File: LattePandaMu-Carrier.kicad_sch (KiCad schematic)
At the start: 0 parts

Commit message: feat: Added hierarchical sheets
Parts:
- added FID78, FID79: Fiducial, symbol Mechanical:Fiducial
- added H1, H2, H3, H4: MountingHole_Pad, symbol Mechanical:MountingHole_Pad
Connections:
- new net GND: H1.1, H2.1, H3.1, H4.1
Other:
- added sheet Fan (fan.kicad_sch)
- added sheet GPIO (gpio.kicad_sch)
- added sheet Gigabit Ethernet (ethernet.kicad_sch)
- added sheet HDMI (hdmi.kicad_sch)
- added sheet LattePanda Module (LattePanda_Module.kicad_sch)
- added sheet M.2 M Key (m2_em_key.kicad_sch)
- added sheet PCIe x4 (picex4.kicad_sch)
- added sheet Power Supply (psu.kicad_sch)
- added sheet USB 2.0 & 3.0 (usb_2_3.kicad_sch)

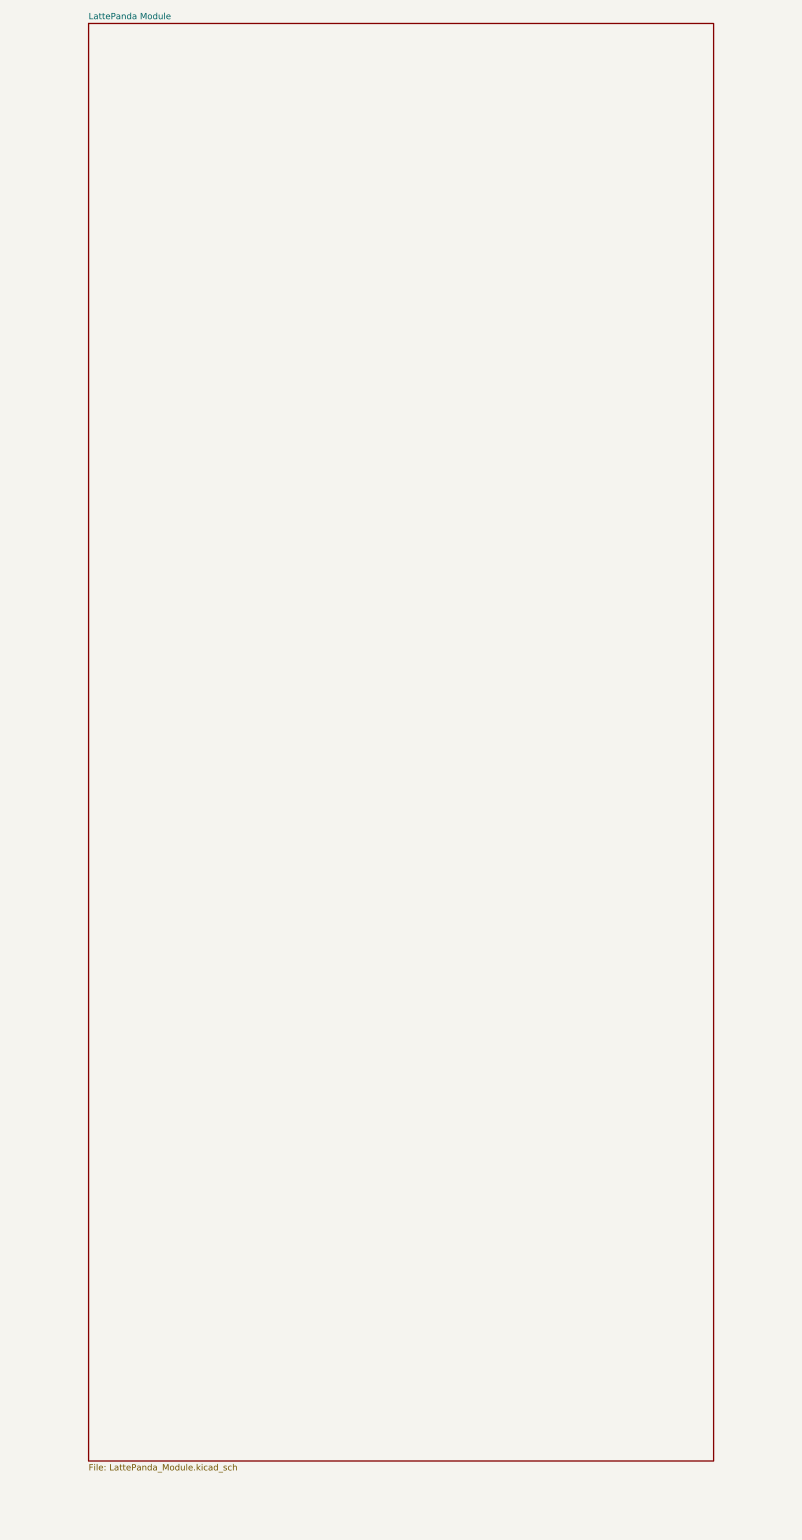
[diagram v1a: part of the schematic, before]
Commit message: feat: Added hierarchical sheets and pins
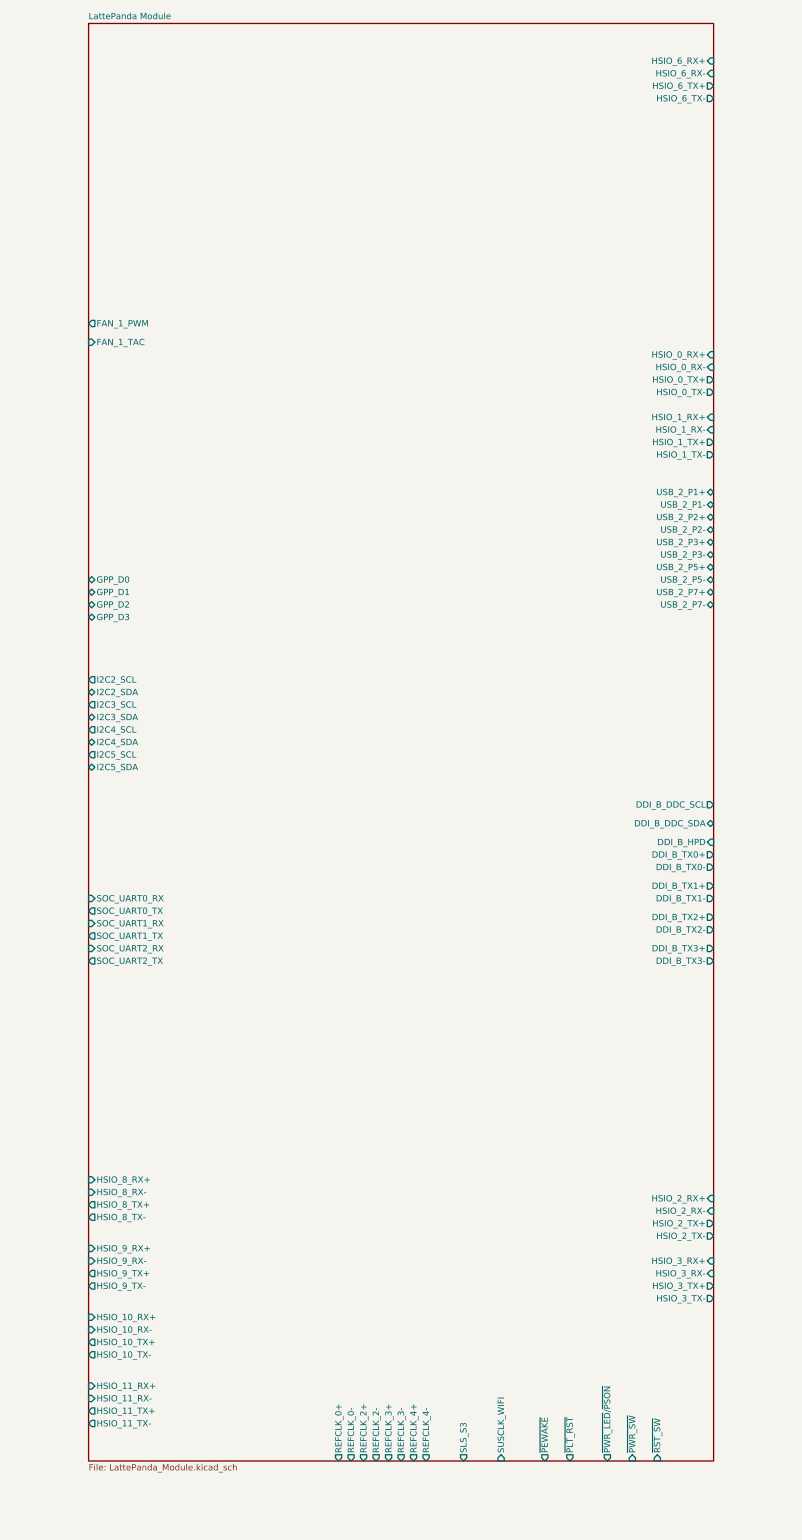
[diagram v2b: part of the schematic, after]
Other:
- sheet LattePanda Module ports: added DDI_B_DDC_SCL, DDI_B_DDC_SDA, DDI_B_HPD, DDI_B_TX0+, DDI_B_TX0-, DDI_B_TX1+, DDI_B_TX1-, DDI_B_TX2+, DDI_B_TX2-, DDI_B_TX3+, DDI_B_TX3-, FAN_1_PWM, FAN_1_TAC, GPP_D0, GPP_D1, GPP_D2, GPP_D3, HSIO_0_RX+, HSIO_0_RX-, HSIO_0_TX+, HSIO_0_TX-, HSIO_10_RX+, HSIO_10_RX-, HSIO_10_TX+, HSIO_10_TX-, HSIO_11_RX+, HSIO_11_RX-, HSIO_11_TX+, HSIO_11_TX-, HSIO_1_RX+, HSIO_1_RX-, HSIO_1_TX+, HSIO_1_TX-, HSIO_2_RX+, HSIO_2_RX-, HSIO_2_TX+, HSIO_2_TX-, HSIO_3_RX+, HSIO_3_RX-, HSIO_3_TX+, HSIO_3_TX-, HSIO_6_RX+, HSIO_6_RX-, HSIO_6_TX+, HSIO_6_TX-, HSIO_8_RX+, HSIO_8_RX-, HSIO_8_TX+, HSIO_8_TX-, HSIO_9_RX+, HSIO_9_RX-, HSIO_9_TX+, HSIO_9_TX-, I2C2_SCL, I2C2_SDA, I2C3_SCL, I2C3_SDA, I2C4_SCL, I2C4_SDA, I2C5_SCL, I2C5_SDA, REFCLK_0+, REFCLK_0-, REFCLK_2+, REFCLK_2-, REFCLK_3+, REFCLK_3-, REFCLK_4+, REFCLK_4-, SLS_S3, SOC_UART0_RX, SOC_UART0_TX, SOC_UART1_RX, SOC_UART1_TX, SOC_UART2_RX, SOC_UART2_TX, SUSCLK_WIFI, USB_2_P1+, USB_2_P1-, USB_2_P2+, USB_2_P2-, USB_2_P3+, USB_2_P3-, USB_2_P5+, USB_2_P5-, USB_2_P7+, USB_2_P7-, ~{PEWAKE}, ~{PLT_RST}, ~{PWR_LED}/~{PSON}, ~{PWR_SW}, ~{RST_SW}; removed none

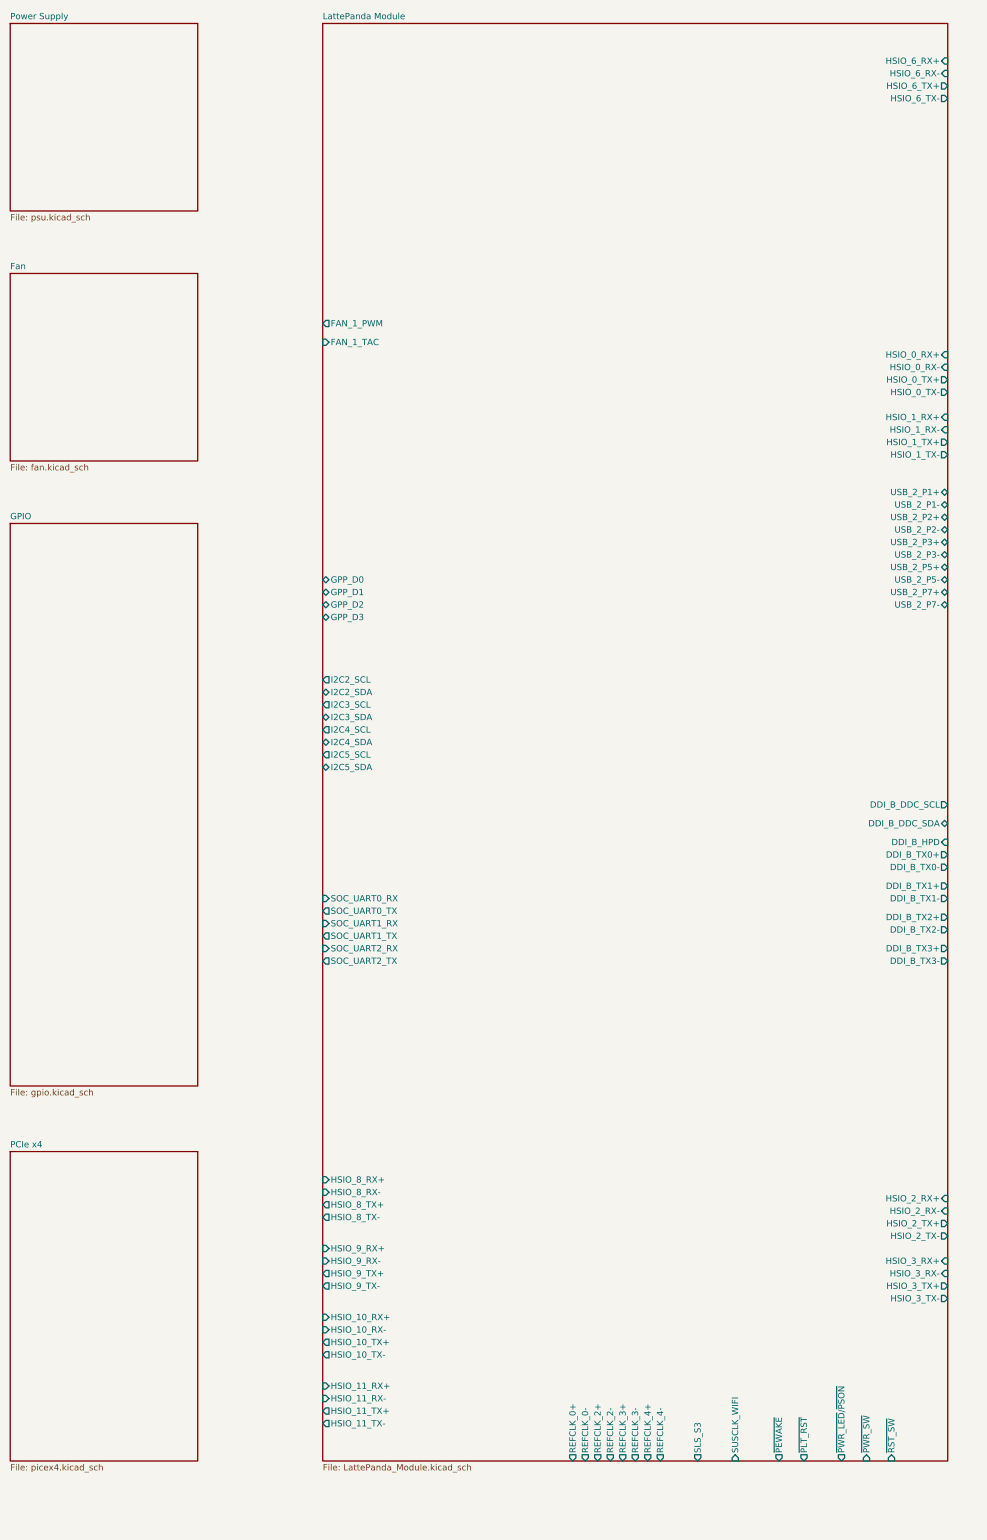
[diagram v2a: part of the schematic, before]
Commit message: feat(psu): Connected psu hierarchical pins to LattePanda sheet
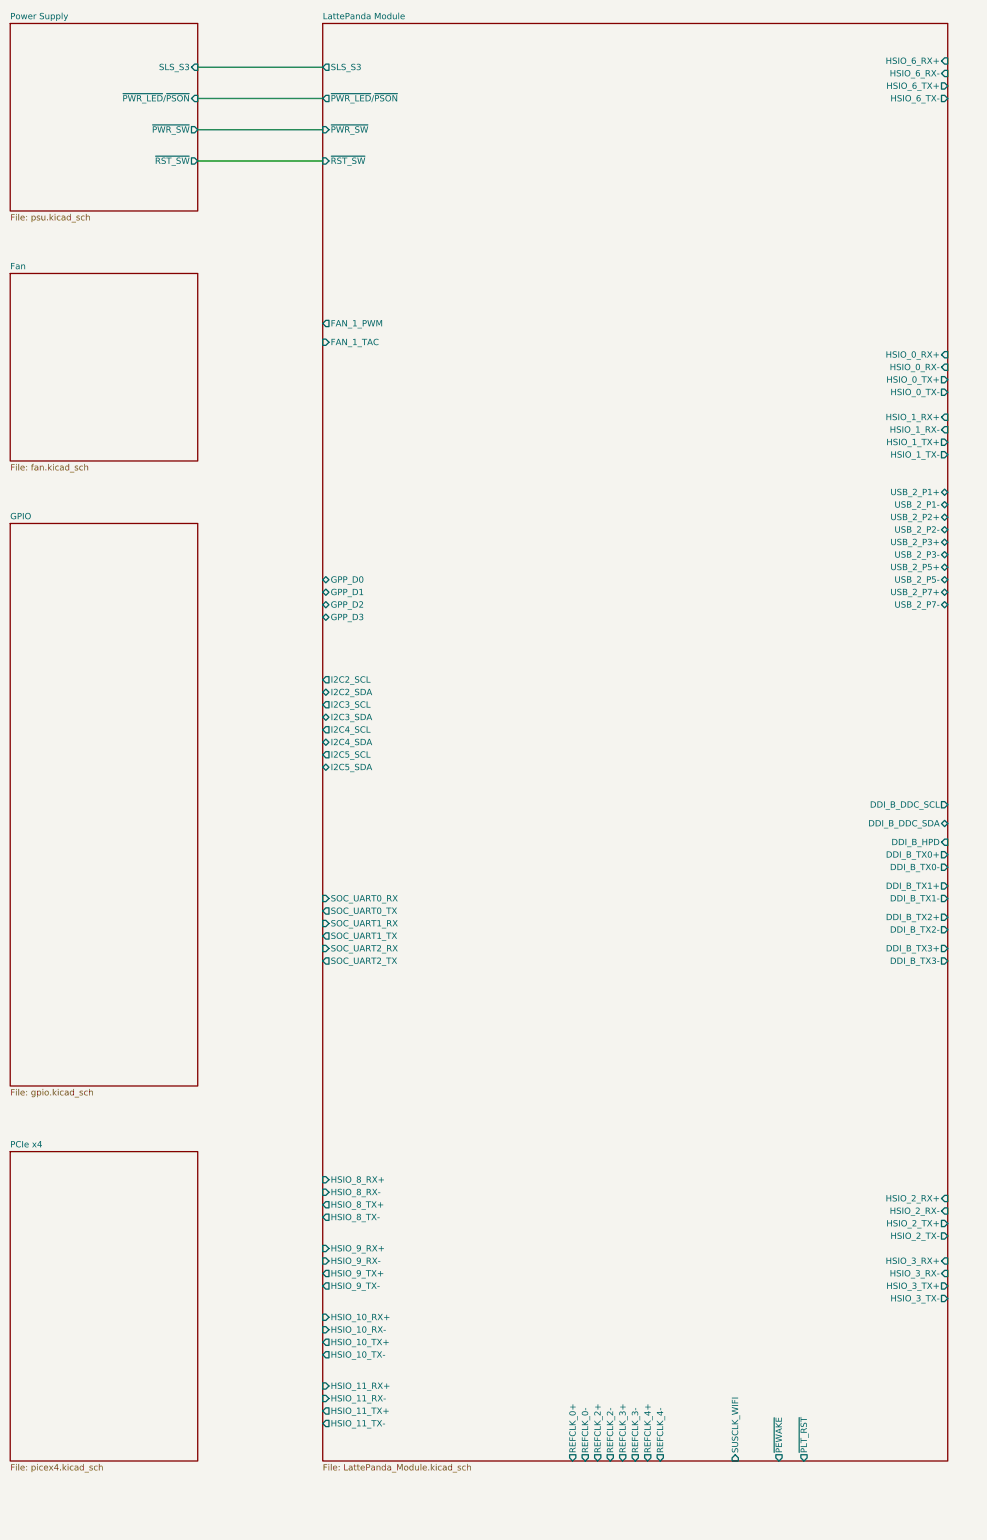
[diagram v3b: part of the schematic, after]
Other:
- sheet Power Supply ports: added SLS_S3, ~{PWR_LED}/~{PSON}, ~{PWR_SW}, ~{RST_SW}; removed none
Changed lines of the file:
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@@
 		(rev "1")
+	)
+	(wire
+		(pts
+			(xy 165.1 66.04) (xy 190.5 66.04)
+		)
+		(stroke
+			(width 0)
+			(type default)
+		)
+	)
+	(wire
+		(pts
+			(xy 165.1 78.74) (xy 190.5 78.74)
+		)
+		(stroke
+			(width 0)
+			(type default)
+		)
+	)
+	(wire
+		(pts
+			(xy 165.1 59.69) (xy 190.5 59.69)
+		)
+		(stroke
+			(width 0)
+			(type default)
+		)
+	)
+	(wire
+		(pts
+			(xy 165.1 72.39) (xy 190.5 72.39)
+		)
+		(stroke
+			(width 0)
+			(type default)
+		)
 	)
 	(symbol
@@
 			)
 		)
+		(pin "SLS_S3" input
+			(at 165.1 59.69 0)
+			(effects
+				(font
+					(size 1.27 1.27)
+				)
+				(justify right)
+			)
+		)
+		(pin "~{PWR_LED}{slash}~{PSON}" input
+			(at 165.1 66.04 0)
+			(effects
+				(font
+					(size 1.27 1.27)
+				)
+				(justify right)
+			)
+		)
+		(pin "~{PWR_SW}" output
+			(at 165.1 72.39 0)
+			(effects
+				(font
+					(size 1.27 1.27)
+				)
+				(justify right)
+			)
+		)
+		(pin "~{RST_SW}" output
+			(at 165.1 78.74 0)
+			(effects
+				(font
+					(size 1.27 1.27)
+				)
+				(justify right)
+			)
+		)
 		(instances
 			(project "LattePandaMu-Carrier"
@@
 		)
 		(pin "SLS_S3" output
-			(at 266.7 342.9 270)
+			(at 190.5 59.69 180)
 			(effects
 				(font
@@
 		)
 		(pin "~{PWR_LED}{slash}~{PSON}" output
-			(at 295.91 342.9 270)
+			(at 190.5 66.04 180)
 			(effects
 				(font
@@
 		)
 		(pin "~{PWR_SW}" input
-			(at 300.99 342.9 270)
+			(at 190.5 72.39 180)
 			(effects
 				(font
@@
 		)
 		(pin "~{RST_SW}" input
-			(at 306.07 342.9 270)
-			(effects
-				(font
+			(at 190.5 78.74 180)
+			(effects
+				(font

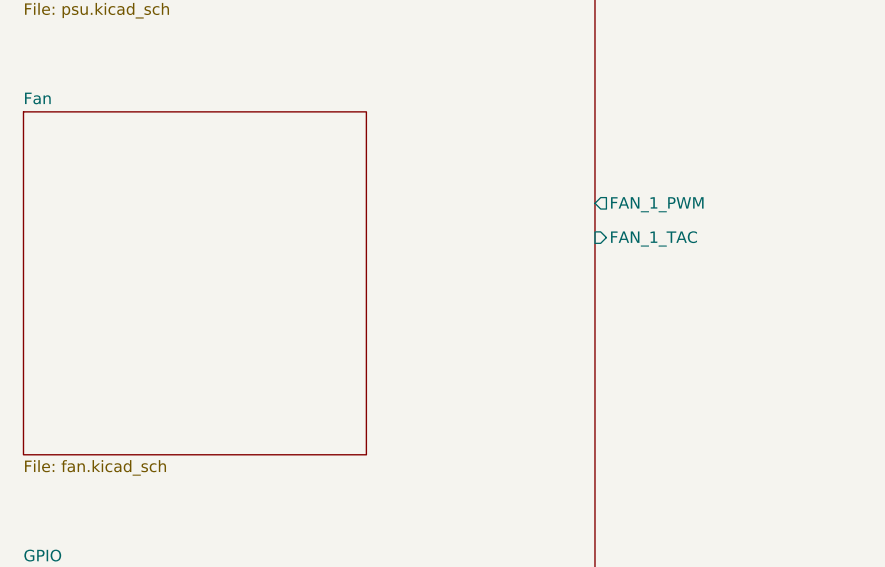
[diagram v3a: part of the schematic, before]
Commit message: feat(fan): Added fan circuit and connected sheet pins
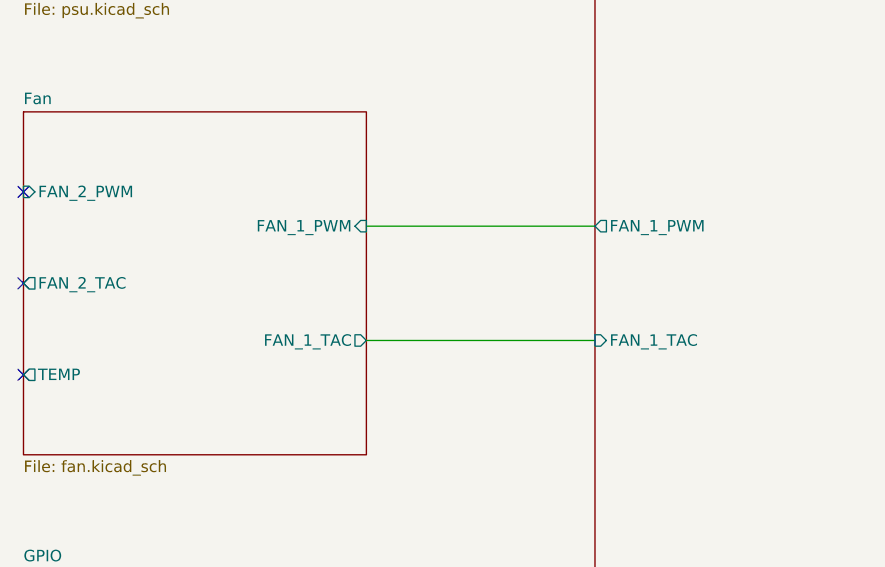
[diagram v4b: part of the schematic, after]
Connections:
- no-connect marks 0 -> 3
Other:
- sheet Fan ports: added FAN_1_PWM, FAN_1_TAC, FAN_2_PWM, FAN_2_TAC, TEMP; removed none
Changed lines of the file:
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@@
 		(rev "1")
+	)
+	(no_connect
+		(at 127 120.65)
+	)
+	(no_connect
+		(at 127 110.49)
+	)
+	(no_connect
+		(at 127 130.81)
 	)
 	(wire
@@
 	(wire
 		(pts
+			(xy 165.1 114.3) (xy 190.5 114.3)
+		)
+		(stroke
+			(width 0)
+			(type default)
+		)
+	)
+	(wire
+		(pts
 			(xy 165.1 78.74) (xy 190.5 78.74)
+		)
+		(stroke
+			(width 0)
+			(type default)
+		)
+	)
+	(wire
+		(pts
+			(xy 165.1 127) (xy 190.5 127)
 		)
 		(stroke
@@
 			)
 		)
+		(pin "FAN_1_PWM" input
+			(at 165.1 114.3 0)
+			(effects
+				(font
+					(size 1.27 1.27)
+				)
+				(justify right)
+			)
+		)
+		(pin "FAN_1_TAC" output
+			(at 165.1 127 0)
+			(effects
+				(font
+					(size 1.27 1.27)
+				)
+				(justify right)
+			)
+		)
+		(pin "FAN_2_PWM" input
+			(at 127 110.49 180)
+			(effects
+				(font
+					(size 1.27 1.27)
+				)
+				(justify left)
+			)
+		)
+		(pin "FAN_2_TAC" output
+			(at 127 120.65 180)
+			(effects
+				(font
+					(size 1.27 1.27)
+				)
+				(justify left)
+			)
+		)
+		(pin "TEMP" output
+			(at 127 130.81 180)
+			(effects
+				(font
+					(size 1.27 1.27)
+				)
+				(justify left)
+			)
+		)
 		(instances
 			(project "LattePandaMu-Carrier"
@@
 		)
 		(pin "FAN_1_PWM" output
-			(at 190.5 111.76 180)
+			(at 190.5 114.3 180)
 			(effects
 				(font
@@
 		)
 		(pin "FAN_1_TAC" input
-			(at 190.5 115.57 180)
-			(effects
-				(font
+			(at 190.5 127 180)
+			(effects
+				(font

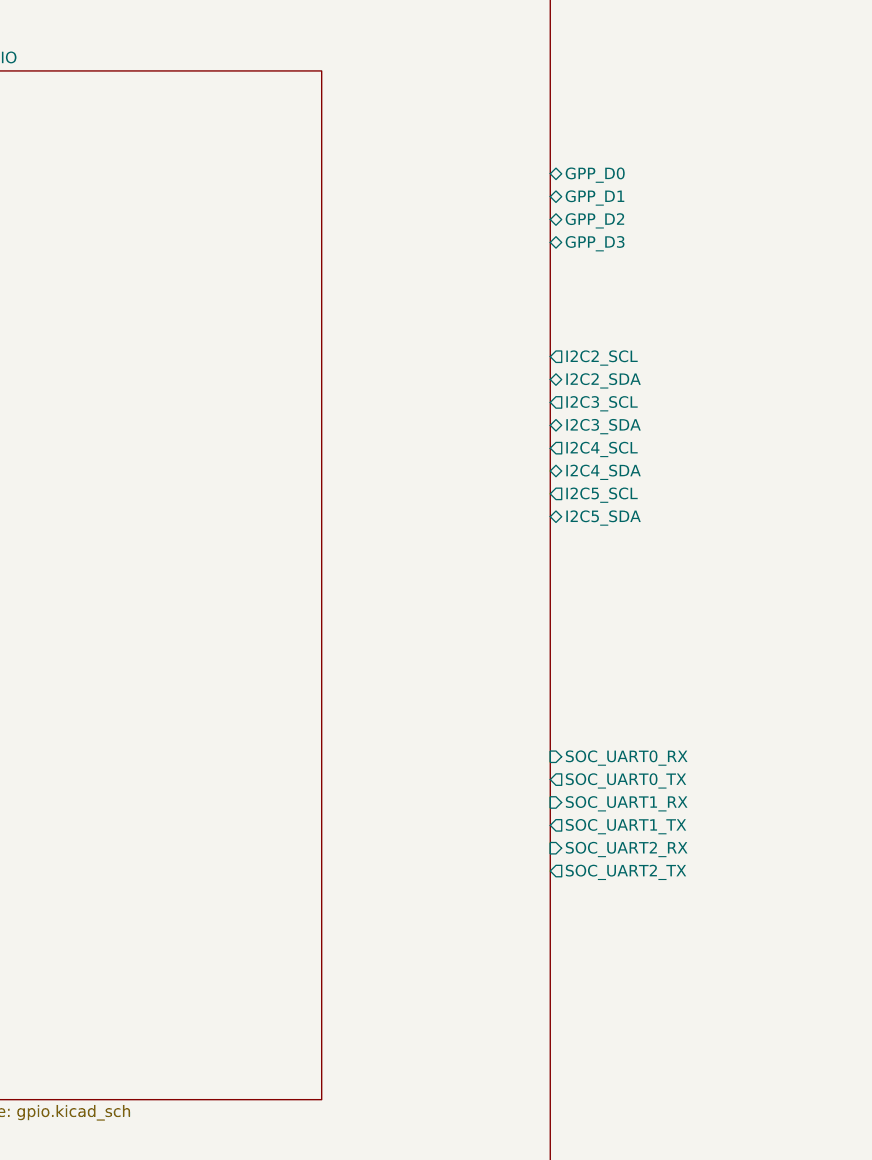
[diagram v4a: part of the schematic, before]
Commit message: feat(gpio): Added gpio circuit and connections
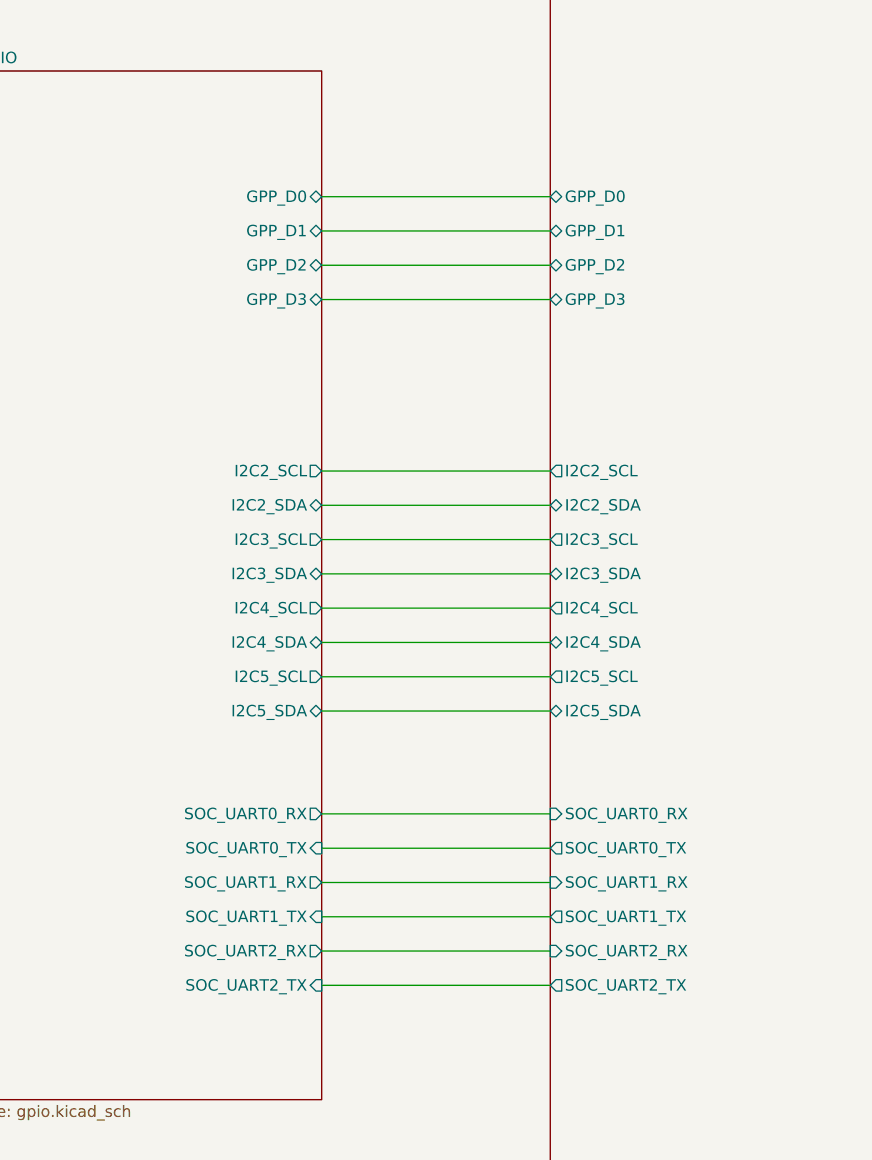
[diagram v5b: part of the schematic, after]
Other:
- sheet GPIO ports: added GPP_D0, GPP_D1, GPP_D2, GPP_D3, I2C2_SCL, I2C2_SDA, I2C3_SCL, I2C3_SDA, I2C4_SCL, I2C4_SDA, I2C5_SCL, I2C5_SDA, SOC_UART0_RX, SOC_UART0_TX, SOC_UART1_RX, SOC_UART1_TX, SOC_UART2_RX, SOC_UART2_TX; removed none
